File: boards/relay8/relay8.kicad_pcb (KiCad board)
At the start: 2 copper layers, 232 x 110 mm, 65 parts, among them J1 USB-C, J11 CH1, J12 CH2, J13 CH3, J14 CH4, J15 CH5, J16 CH6, J17 CH7, J18 CH8, J2 UART, J20 MAINS IN, K1 SRD-05VDC-SL-C, K2 SRD-05VDC-SL-C, K3 SRD-05VDC-SL-C, K4 SRD-05VDC-SL-C, K5 SRD-05VDC-SL-C, K6 SRD-05VDC-SL-C, K7 SRD-05VDC-SL-C, K8 SRD-05VDC-SL-C, Q1 AO3401A, SW1 RESET, SW2 BOOT, U1 ESP32-C3-WROOM-02-N4, U2 LP38693MP-3.3, U3 ULN2803A

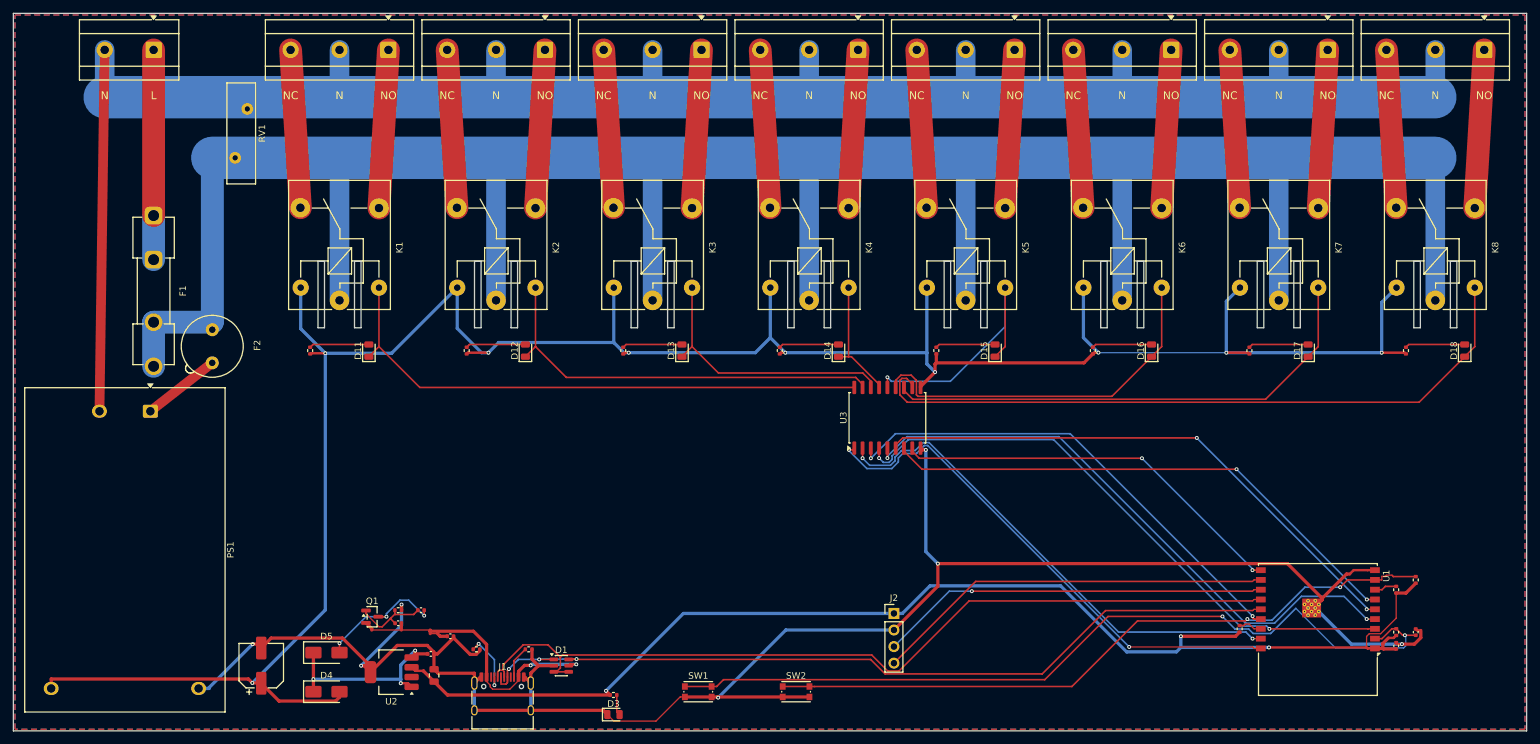
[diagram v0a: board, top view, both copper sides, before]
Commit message: pcbgen: UUIDs derived from the design so routing is the same on every KiCad 10.0.x (#11)
KIID.SeedGenerator alone is not enough: KiCad 10.0.6 and 10.0.7 consume a
different number of UUIDs while loading footprints, the Specctra exporter
orders by UUID, and freerouting gave 6 vias locally vs 9 on CI.
stable_uuids() sets every item to uuid5(board/ref/kind/index) before each
save that feeds routing. esp32c3: C4 moved 0.66 mm and turned 270 deg; EN
did not route in the new order.
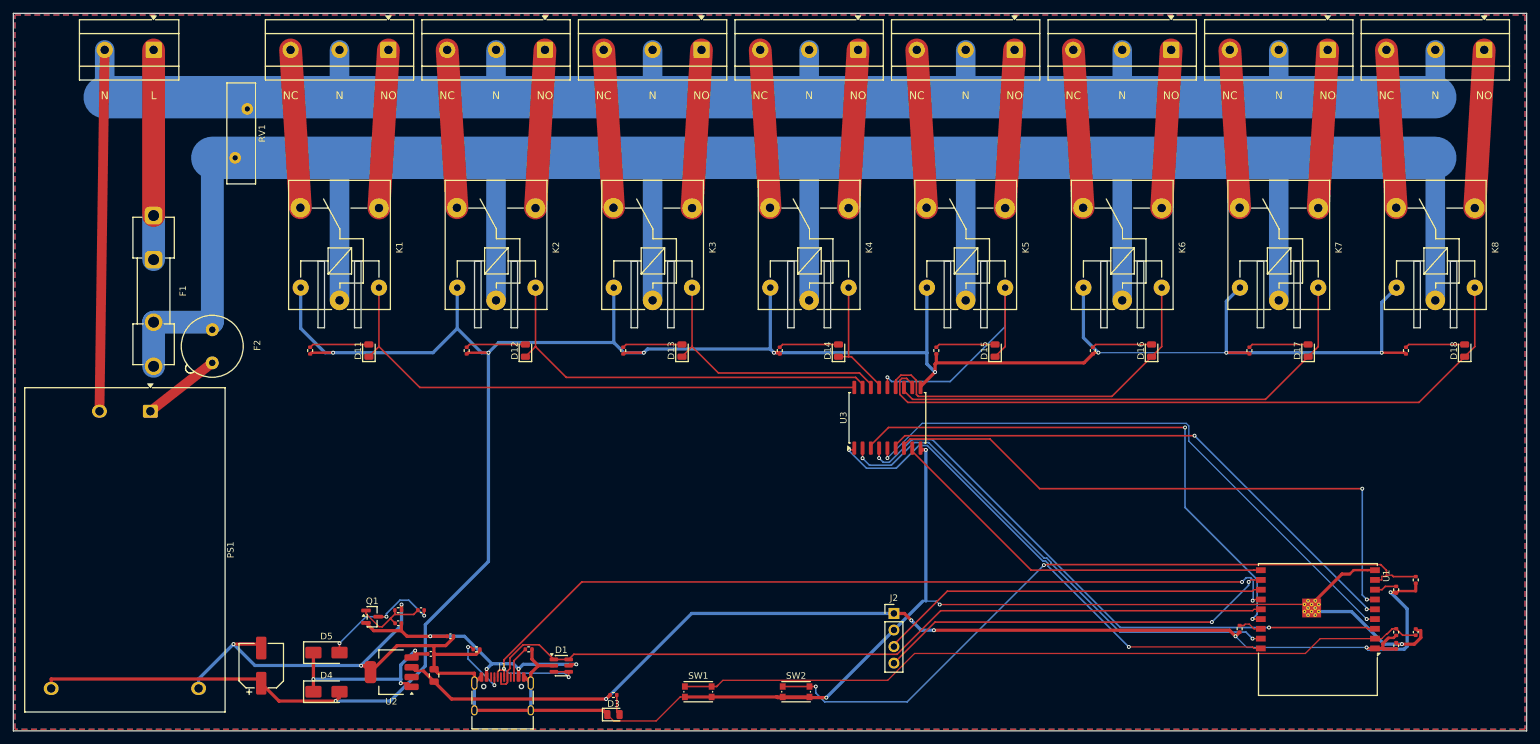
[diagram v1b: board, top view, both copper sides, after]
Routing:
- net 5V_PS: track 374.6 -> 388.7 mm
- net EN: track 129.3 -> 116.1 mm, vias 2 -> 0
- net IN7: track 82.1 -> 92.8 mm
- net IN3: track 74.8 -> 85.3 mm
- net USB_DN: track 132.7 -> 142.8 mm, vias 0 -> 4
- net GND: track 318.5 -> 309.0 mm
- net +3V3: track 194.7 -> 186.8 mm, vias 3 -> 6
- net IO9: track 104.7 -> 110.9 mm
- net VBUS: track 48.0 -> 44.1 mm, vias 2 -> 4
- net USB_DP: track 129.9 -> 126.2 mm, vias 3 -> 0
- net RXD: track 61.5 -> 61.8 mm, vias 0 -> 2
- net TXD: track 59.9 -> 60.0 mm, vias 1 -> 0
- net IN8: track 61.6 -> 61.5 mm, vias 2 -> 0
